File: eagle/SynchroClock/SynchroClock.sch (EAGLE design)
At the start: 38 parts, among them IC1 MCP1702-18, IC2 DS3231/SO, J1 VIN, U1 TC1262, U2 DRV8838, U3 ATTINY85-P

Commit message: switch to 1.5v for clock voltage regulator
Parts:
- IC1: value MCP1702-18 -> MCP1702-15
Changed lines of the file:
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@@
 <?xml version="1.0" encoding="utf-8"?>
 <!DOCTYPE eagle SYSTEM "eagle.dtd">
-<eagle version="8.2.1">
+<eagle version="8.2.2">
 <drawing>
 <settings>
@@
 <part name="+3V313" library="supply1" library_urn="urn:adsk.eagle:library:371" deviceset="+3V3" device=""/>
 <part name="GND12" library="supply1" library_urn="urn:adsk.eagle:library:371" deviceset="GND" device=""/>
-<part name="IC1" library="SynchroClock" deviceset="MCP1702" device="INLINE" value="MCP1702-18"/>
+<part name="IC1" library="SynchroClock" deviceset="MCP1702" device="INLINE" value="MCP1702-15"/>
 <part name="GND13" library="supply1" library_urn="urn:adsk.eagle:library:371" deviceset="GND" device=""/>
 <part name="+3V315" library="supply1" library_urn="urn:adsk.eagle:library:371" deviceset="+3V3" device=""/>
@@
 <part name="C4" library="capacitor-wima" library_urn="urn:adsk.eagle:library:116" deviceset="C" device="2.5/2" value="0.1uf"/>
 <part name="GND4" library="supply1" library_urn="urn:adsk.eagle:library:371" deviceset="GND" device=""/>
-<part name="+3V33" library="SynchroClock" deviceset="+1V8" device=""/>
-<part name="+3V314" library="SynchroClock" deviceset="+1V8" device=""/>
+<part name="+3V33" library="SynchroClock" deviceset="+1V5" device=""/>
+<part name="+3V314" library="SynchroClock" deviceset="+1V5" device=""/>
 <part name="+3V31" library="supply1" library_urn="urn:adsk.eagle:library:371" deviceset="+3V3" device=""/>
 <part name="U1" library="SynchroClock" deviceset="TC1262" device=""/>

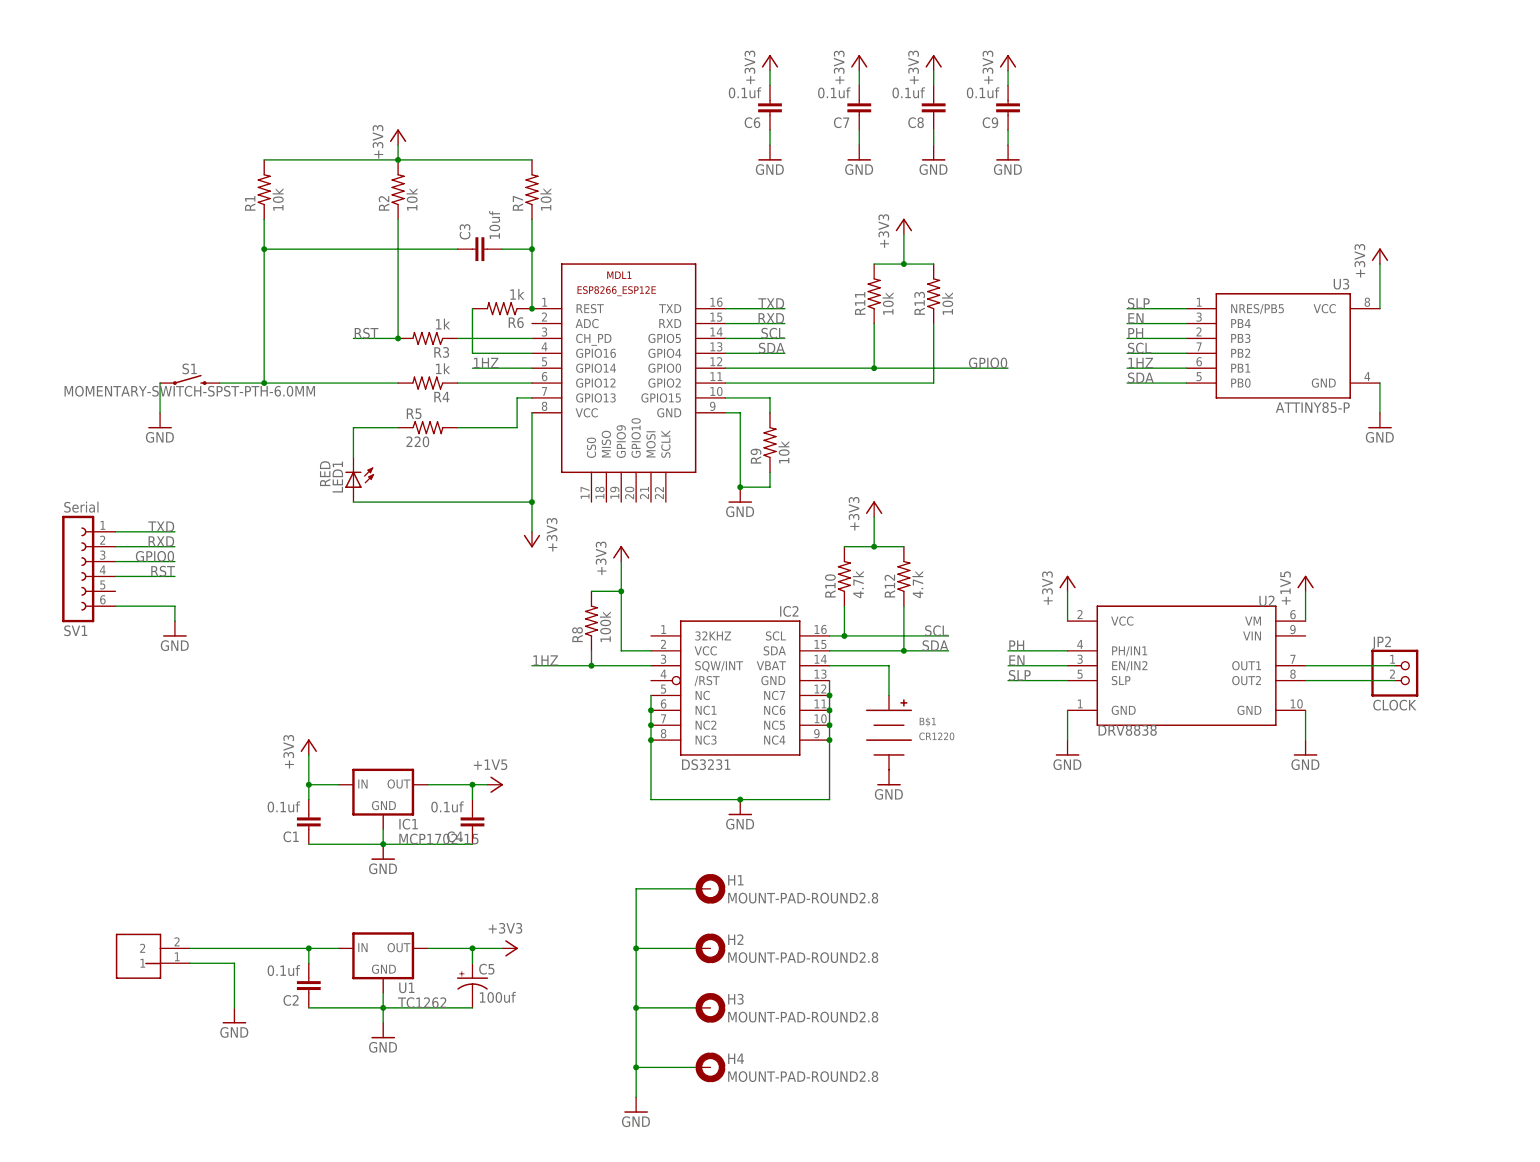
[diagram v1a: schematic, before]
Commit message: "development" version - board that does not have the clock driver
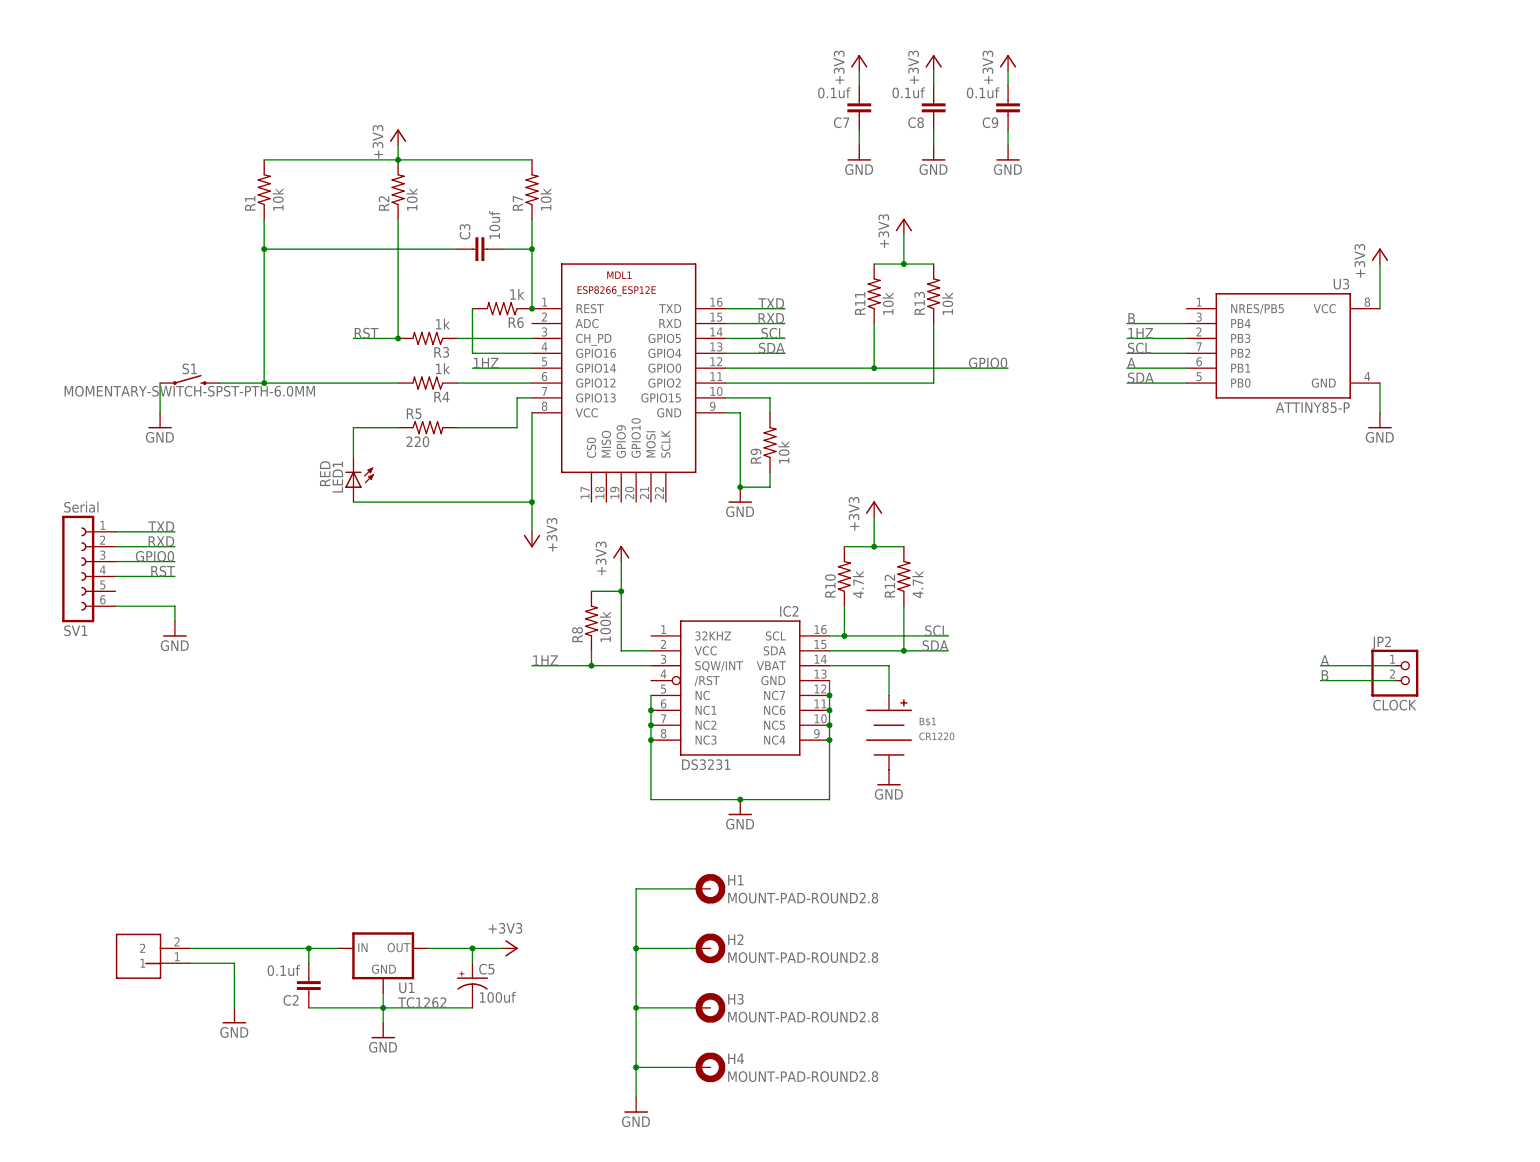
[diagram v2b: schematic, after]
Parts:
- removed C1, C4, C6: 0.1uf, capacitor-wima:C2.5/2
- removed IC1: MCP1702-15, SynchroClock:MCP1702INLINE
- removed U2: DRV8838, SynchroClock:DRV883X-POLULU
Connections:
- removed net +1V8: C4.2, IC1.OUT, U2.VM
- removed net EN: U2.EN/IN2, U3.PB4
- removed net N$12: JP2.1, U2.OUT1
- removed net N$13: JP2.2, U2.OUT2
- removed net PH: U2.PH/IN1, U3.PB3
- removed net SLP: U2.SLP, U3.NRES/PB5
- new net A: JP2.1, U3.PB1
- new net B: JP2.2, U3.PB4
- net +3V3: no longer C1.2, C6.2, IC1.IN, U2.VCC
- net 1HZ: now also U3.PB3; no longer U3.PB1
- net GND: no longer C1.1, C4.1, C6.1, IC1.GND, U2.GND@1, U2.GND@2

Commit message: Alpha 2.0 board
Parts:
- removed C7, C8, C9: 0.1uf, capacitor-wima:C2.5/2
- removed U3: ATTINY85-P, SynchroClock:ATTINY85-P
- added C1: 10uf, capacitor-wima:C5/2.5
- added C4, C6: 0.1uf, capacitor-wima:C2.5/2
- added ISP1: AVRISP-6, SynchroClock:AVRISP-6
- added JP1: PWF, SynchroClock:JUMPER-2PTH
- added JP3: ATVCC, SynchroClock:JUMPER-2PTH
- added R14, R15: 100, resistor:R-US_0204/2V
- added U2: ATTINY85-P, SynchroClock:ATTINY85-P
- C3: value 10uf -> 100uf; device capacitor-wima:C2.5/2 -> rcl:CPOL-USE2.5-5
- C5: value 100uf -> 0.1uf; device rcl:CPOL-USE2.5-5 -> capacitor-wima:C2.5/2
- R11: value 10k -> 4.7k
- R12: value 4.7k -> 10k
- R2, R7: value 10k -> 1k
- R3, R6: value 1k -> 10k
- S1: value MOMENTARY-SWITCH-SPST-PTH-6.0MM -> CONFIG
- renumbered B$1 to B1, IC2 to IC1
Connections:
- net N$10 renamed GPIO2
- net N$8 renamed GPIO15
- removed net N$2: MDL1.GPIO16, R6.2
- removed net N$3: MDL1.CH_PD, R3.1
- removed net N$4: MDL1.GPIO12, R4.1
- removed net N$5: C3.1, R1.1, R4.2, S1.2
- removed net N$7: LED1.C, R5.1
- new net ATVCC: C6.2, JP3.2, U2.VCC
- new net CFG: MDL1.GPIO12, R2.1
- new net CH_PD: MDL1.CH_PD, R7.1
- new net GPIO16: MDL1.GPIO16, R4.1
- new net LED: LED1.C, MDL1.GPIO13
- new net N$11: JP2.2, R15.2
- new net N$9: JP2.1, R14.2
- new net NRES: ISP1.RST, JP1.1, U2.NRES/PB5
- new net NRST: IC1./RST, JP1.2
- new net REST: C1.2, MDL1.REST, R3.1, R4.2
- net +3V3: now also C3.+, C4.2, C5.2, ISP1.VCC, JP3.1, R3.2, R5.2, R6.2; no longer C5.+, C7.2, C8.2, C9.2, LED1.A, R2.2, R7.2, U3.VCC
- net 1HZ: now also U2.PB3; no longer U3.PB3
- net A: now also ISP1.MISO, R14.1, U2.PB1; no longer JP2.1, U3.PB1
- net B: now also R15.1, U2.PB4; no longer JP2.2, U3.PB4
- net GND: now also C3.-, C4.1, C5.1, C6.1, ISP1.GND, U2.GND; no longer C5.-, C7.1, C8.1, C9.1, U3.GND
- net GPIO0: now also R12.1; no longer R11.1
- net N$1: now also C1.1, R1.1, R2.2, S1.2; no longer C3.2, MDL1.REST, R6.1, R7.1
- net N$6: now also LED1.A, R5.1; no longer MDL1.GPIO13, R5.2
- net RST: now also R6.1, R7.2; no longer R2.1, R3.2
- net SCL: now also ISP1.SCK, U2.PB2; no longer U3.PB2
- net SDA: now also ISP1.MOSI, R11.1, U2.PB0; no longer R12.1, U3.PB0
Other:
- moved on the sheet: JP2, LED1, MDL1, R1, R11, R12, R13, R2, R3, R4, R5, R6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

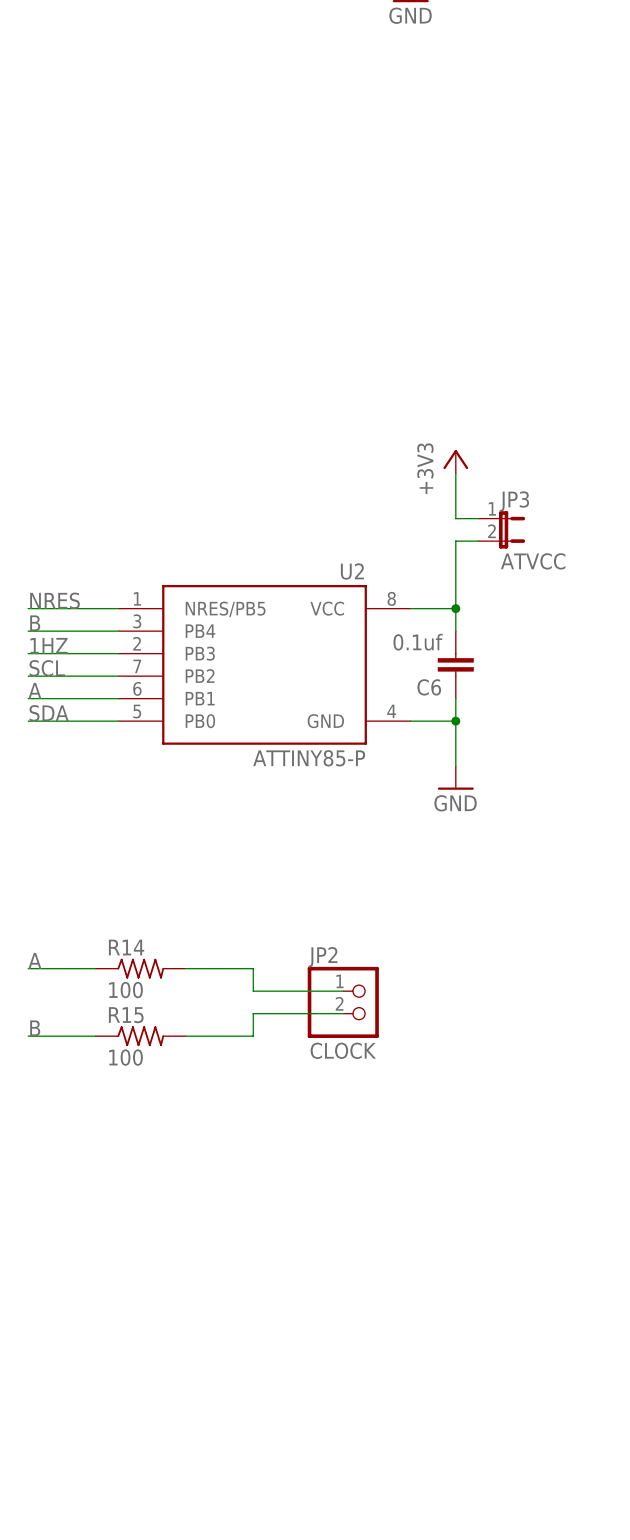
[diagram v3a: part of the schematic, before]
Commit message: added power fail circuit for ATtiny85 added BOM save all clock properties at power fail
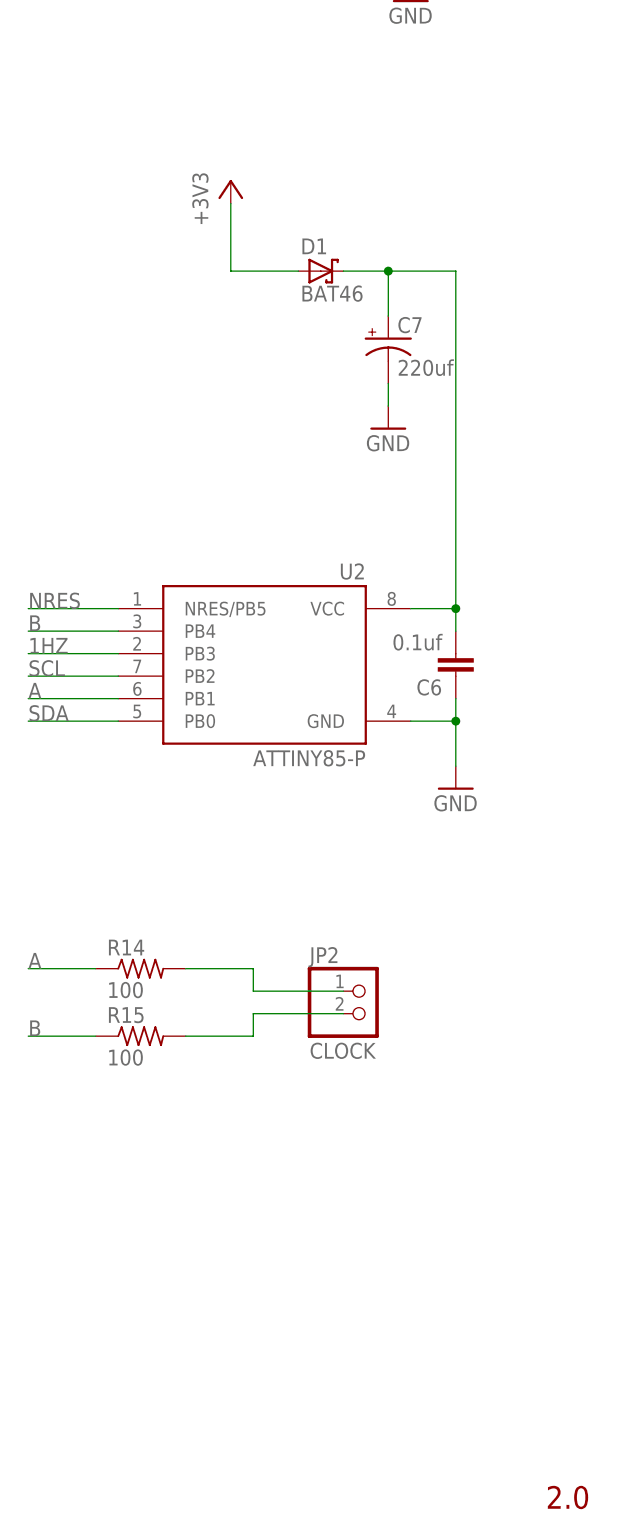
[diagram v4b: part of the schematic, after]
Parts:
- removed JP3: ATVCC, SynchroClock:JUMPER-2PTH
- added C7: 220uf, rcl:CPOL-USE2.5-5
- added D1: BAT46, SynchroClock:BAT46
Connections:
- net +3V3: now also D1.A; no longer JP3.1
- net ATVCC: now also C7.+, D1.C; no longer JP3.2
- net GND: now also C7.-
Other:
- note added: "2.0"
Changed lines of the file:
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@@
 <part name="R9" library="resistor" library_urn="urn:adsk.eagle:library:348" deviceset="R-US_" device="0204/2V" value="10k"/>
 <part name="GND2" library="supply1" library_urn="urn:adsk.eagle:library:371" deviceset="GND" device=""/>
-<part name="+3V310" library="supply1" library_urn="urn:adsk.eagle:library:371" deviceset="+3V3" device=""/>
 <part name="GND11" library="supply1" library_urn="urn:adsk.eagle:library:371" deviceset="GND" device=""/>
 <part name="U1" library="SynchroClock" deviceset="TC1262" device=""/>
@@
 <part name="R14" library="resistor" library_urn="urn:adsk.eagle:library:348" deviceset="R-US_" device="0204/2V" value="100"/>
 <part name="R15" library="resistor" library_urn="urn:adsk.eagle:library:348" deviceset="R-US_" device="0204/2V" value="100"/>
-<part name="JP3" library="SynchroClock" deviceset="JUMPER-2" device="PTH" value="ATVCC"/>
 <part name="JP1" library="SynchroClock" deviceset="JUMPER-2" device="PTH" value="PWF"/>
 <part name="ISP1" library="SynchroClock" deviceset="AVRISP" device="-6"/>
@@
 <part name="+3V31" library="supply1" library_urn="urn:adsk.eagle:library:371" deviceset="+3V3" device=""/>
 <part name="+3V32" library="supply1" library_urn="urn:adsk.eagle:library:371" deviceset="+3V3" device=""/>
+<part name="D1" library="SynchroClock" deviceset="BAT46" device=""/>
+<part name="C7" library="rcl" library_urn="urn:adsk.eagle:library:334" deviceset="CPOL-US" device="E2.5-5" value="220uf"/>
+<part name="+3V1" library="supply1" library_urn="urn:adsk.eagle:library:371" deviceset="+3V3" device=""/>
+<part name="GND12" library="supply1" library_urn="urn:adsk.eagle:library:371" deviceset="GND" device=""/>
 </parts>
 <sheets>
 <sheet>
 <plain>
+<text x="264.16" y="7.62" size="2.54" layer="94">2.0</text>
 </plain>
 <instances>
@@
 <instance part="R9" gate="G$1" x="152.4" y="147.32" rot="R90"/>
 <instance part="GND2" gate="1" x="40.64" y="78.74"/>
-<instance part="+3V310" gate="G$1" x="254" y="127"/>
 <instance part="GND11" gate="1" x="254" y="88.9"/>
 <instance part="U1" gate="G$1" x="76.2" y="40.64"/>
@@
 <instance part="R14" gate="G$1" x="218.44" y="68.58"/>
 <instance part="R15" gate="G$1" x="218.44" y="60.96"/>
-<instance part="JP3" gate="A" x="259.08" y="119.38" rot="R270"/>
 <instance part="JP1" gate="A" x="81.28" y="88.9"/>
 <instance part="ISP1" gate="G$1" x="228.6" y="187.96"/>
@@
 <instance part="+3V31" gate="G$1" x="40.64" y="195.58"/>
 <instance part="+3V32" gate="G$1" x="58.42" y="142.24"/>
+<instance part="D1" gate="1" x="238.76" y="147.32"/>
+<instance part="C7" gate="G$1" x="246.38" y="139.7"/>
+<instance part="+3V1" gate="G$1" x="228.6" y="157.48"/>
+<instance part="GND12" gate="1" x="246.38" y="129.54"/>
 </instances>
 <busses>
@@
 </segment>
 <segment>
-<pinref part="JP3" gate="A" pin="1"/>
-<wire x1="256.54" y1="119.38" x2="254" y2="119.38" width="0.1524" layer="91"/>
-<pinref part="+3V310" gate="G$1" pin="+3V3"/>
-<wire x1="254" y1="119.38" x2="254" y2="124.46" width="0.1524" layer="91"/>
-</segment>
-<segment>
 <pinref part="ISP1" gate="G$1" pin="VCC"/>
 <wire x1="243.84" y1="190.5" x2="248.92" y2="190.5" width="0.1524" layer="91"/>
@@
 <pinref part="+3V32" gate="G$1" pin="+3V3"/>
 <wire x1="58.42" y1="134.62" x2="58.42" y2="139.7" width="0.1524" layer="91"/>
+</segment>
+<segment>
+<pinref part="+3V1" gate="G$1" pin="+3V3"/>
+<wire x1="228.6" y1="154.94" x2="228.6" y2="147.32" width="0.1524" layer="91"/>
+<pinref part="D1" gate="1" pin="A"/>
+<wire x1="228.6" y1="147.32" x2="236.22" y2="147.32" width="0.1524" layer="91"/>
 </segment>
 </net>
@@
 <wire x1="248.92" y1="185.42" x2="248.92" y2="180.34" width="0.1524" layer="91"/>
 </segment>
+<segment>
+<pinref part="C7" gate="G$1" pin="-"/>
+<pinref part="GND12" gate="1" pin="GND"/>
+<wire x1="246.38" y1="134.62" x2="246.38" y2="132.08" width="0.1524" layer="91"/>
+</segment>
 </net>
 <net name="1HZ" class="0">
@@
 <net name="ATVCC" class="1">
 <segment>
+<pinref part="D1" gate="1" pin="C"/>
+<wire x1="241.3" y1="147.32" x2="246.38" y2="147.32" width="0.1524" layer="91"/>
+<pinref part="C7" gate="G$1" pin="+"/>
+<wire x1="246.38" y1="147.32" x2="254" y2="147.32" width="0.1524" layer="91"/>
+<wire x1="246.38" y1="142.24" x2="246.38" y2="147.32" width="0.1524" layer="91"/>
+<junction x="246.38" y="147.32"/>
 <pinref part="C6" gate="G$1" pin="2"/>
 <pinref part="U2" gate="G$1" pin="VCC"/>
 <wire x1="254" y1="109.22" x2="254" y2="106.68" width="0.1524" layer="91"/>
 <wire x1="248.92" y1="109.22" x2="254" y2="109.22" width="0.1524" layer="91"/>
-<pinref part="JP3" gate="A" pin="2"/>
-<wire x1="256.54" y1="116.84" x2="254" y2="116.84" width="0.1524" layer="91"/>
-<wire x1="254" y1="116.84" x2="254" y2="109.22" width="0.1524" layer="91"/>
+<wire x1="254" y1="147.32" x2="254" y2="109.22" width="0.1524" layer="91"/>
 <junction x="254" y="109.22"/>
 </segment>
